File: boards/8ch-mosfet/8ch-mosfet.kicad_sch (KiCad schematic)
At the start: 6 parts, among them U1 ESP32-DEVKITC

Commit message: updated layout with new fuse.
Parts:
- H1, H2, H3, H4, H5: symbol Mechanical:MountingHole -> Mechanical:MountingHole_Pad
- U1: footprint gnarboard:ESP32-DevKitC -> yarrboard:ESP32-DevKitC
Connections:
- no-connect marks 13 -> 18
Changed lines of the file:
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@@
   (no_connect (at 223.52 92.71))
   (no_connect (at 185.42 57.15))
+  (no_connect (at 15.24 195.58))
   (no_connect (at 223.52 97.79))
   (no_connect (at 185.42 95.25))
@@
   (no_connect (at 185.42 59.69))
   (no_connect (at 223.52 64.77))
+  (no_connect (at 15.24 180.34))
   (no_connect (at 223.52 62.23))
+  (no_connect (at 15.24 165.1))
   (no_connect (at 223.52 100.33))
+  (no_connect (at 15.24 172.72))
   (no_connect (at 223.52 87.63))
   (no_connect (at 185.42 67.31))
+  (no_connect (at 15.24 187.96))
   (no_connect (at 223.52 95.25))
   (wire (pts (xy 181.61 62.23) (xy 185.42 62.23))
@@
     )
   )
-  (symbol (lib_id "Mechanical:MountingHole") (at 15.875 184.785 0) (unit 1)
+  (symbol (lib_id "Mechanical:MountingHole_Pad") (at 15.24 177.8 0) (unit 1)
     (in_bom yes) (on_board yes) (dnp no) (fields_autoplaced)
-    (property "Reference" "H3" (at 18.415 183.515 0)
-      (effects (font (size 1.27 1.27)) (justify left))
-    )
-    (property "Value" "MountingHole" (at 18.415 186.055 0)
-      (effects (font (size 1.27 1.27)) (justify left))
-    )
-    (property "Footprint" "MountingHole:MountingHole_3.2mm_M3_DIN965_Pad" (at 15.875 184.785 0)
-      (effects (font (size 1.27 1.27)) hide)
-    )
-    (property "Datasheet" "~" (at 15.875 184.785 0)
-      (effects (font (size 1.27 1.27)) hide)
-    )
+    (property "Reference" "H3" (at 17.78 176.53 0)
+      (effects (font (size 1.27 1.27)) (justify left))
+    )
+    (property "Value" "MountingHole" (at 17.78 179.07 0)
+      (effects (font (size 1.27 1.27)) (justify left))
+    )
+    (property "Footprint" "MountingHole:MountingHole_3.2mm_M3_DIN965_Pad" (at 15.24 177.8 0)
+      (effects (font (size 1.27 1.27)) hide)
+    )
+    (property "Datasheet" "~" (at 15.24 177.8 0)
+      (effects (font (size 1.27 1.27)) hide)
+    )
+    (pin "1")
     (instances
       (project "8ch-mosfet"
@@
     )
   )
-  (symbol (lib_id "Mechanical:MountingHole") (at 15.875 194.945 0) (unit 1)
+  (symbol (lib_id "Mechanical:MountingHole_Pad") (at 15.24 193.04 0) (unit 1)
     (in_bom yes) (on_board yes) (dnp no) (fields_autoplaced)
-    (property "Reference" "H5" (at 18.415 193.675 0)
-      (effects (font (size 1.27 1.27)) (justify left))
-    )
-    (property "Value" "MountingHole" (at 18.415 196.215 0)
-      (effects (font (size 1.27 1.27)) (justify left))
-    )
-    (property "Footprint" "MountingHole:MountingHole_3.2mm_M3_DIN965_Pad" (at 15.875 194.945 0)
-      (effects (font (size 1.27 1.27)) hide)
-    )
-    (property "Datasheet" "~" (at 15.875 194.945 0)
-      (effects (font (size 1.27 1.27)) hide)
-    )
+    (property "Reference" "H5" (at 17.78 191.77 0)
+      (effects (font (size 1.27 1.27)) (justify left))
+    )
+    (property "Value" "MountingHole" (at 17.78 194.31 0)
+      (effects (font (size 1.27 1.27)) (justify left))
+    )
+    (property "Footprint" "MountingHole:MountingHole_3.2mm_M3_DIN965_Pad" (at 15.24 193.04 0)
+      (effects (font (size 1.27 1.27)) hide)
+    )
+    (property "Datasheet" "~" (at 15.24 193.04 0)
+      (effects (font (size 1.27 1.27)) hide)
+    )
+    (pin "1")
     (instances
       (project "8ch-mosfet"
@@
     )
   )
-  (symbol (lib_id "Mechanical:MountingHole") (at 15.875 179.705 0) (unit 1)
+  (symbol (lib_id "Mechanical:MountingHole_Pad") (at 15.24 170.18 0) (unit 1)
     (in_bom yes) (on_board yes) (dnp no) (fields_autoplaced)
-    (property "Reference" "H2" (at 18.415 178.435 0)
-      (effects (font (size 1.27 1.27)) (justify left))
-    )
-    (property "Value" "MountingHole" (at 18.415 180.975 0)
-      (effects (font (size 1.27 1.27)) (justify left))
-    )
-    (property "Footprint" "MountingHole:MountingHole_3.2mm_M3_DIN965_Pad" (at 15.875 179.705 0)
-      (effects (font (size 1.27 1.27)) hide)
-    )
-    (property "Datasheet" "~" (at 15.875 179.705 0)
-      (effects (font (size 1.27 1.27)) hide)
-    )
+    (property "Reference" "H2" (at 17.78 168.91 0)
+      (effects (font (size 1.27 1.27)) (justify left))
+    )
+    (property "Value" "MountingHole" (at 17.78 171.45 0)
+      (effects (font (size 1.27 1.27)) (justify left))
+    )
+    (property "Footprint" "MountingHole:MountingHole_3.2mm_M3_DIN965_Pad" (at 15.24 170.18 0)
+      (effects (font (size 1.27 1.27)) hide)
+    )
+    (property "Datasheet" "~" (at 15.24 170.18 0)
+      (effects (font (size 1.27 1.27)) hide)
+    )
+    (pin "1")
     (instances
       (project "8ch-mosfet"
@@
       (effects (font (size 1.27 1.27)) hide)
     )
-    (property "Footprint" "gnarboard:ESP32-DevKitC" (at 204.47 49.53 0)
+    (property "Footprint" "yarrboard:ESP32-DevKitC" (at 204.47 49.53 0)
       (effects (font (size 1.27 1.27)))
     )
@@
     )
   )
-  (symbol (lib_id "Mechanical:MountingHole") (at 15.875 174.625 0) (unit 1)
+  (symbol (lib_id "Mechanical:MountingHole_Pad") (at 15.24 162.56 0) (unit 1)
     (in_bom yes) (on_board yes) (dnp no) (fields_autoplaced)
-    (property "Reference" "H1" (at 18.415 173.355 0)
-      (effects (font (size 1.27 1.27)) (justify left))
-    )
-    (property "Value" "MountingHole" (at 18.415 175.895 0)
-      (effects (font (size 1.27 1.27)) (justify left))
-    )
-    (property "Footprint" "MountingHole:MountingHole_3.2mm_M3_DIN965_Pad" (at 15.875 174.625 0)
-      (effects (font (size 1.27 1.27)) hide)
-    )
-    (property "Datasheet" "~" (at 15.875 174.625 0)
-      (effects (font (size 1.27 1.27)) hide)
-    )
+    (property "Reference" "H1" (at 17.78 161.29 0)
+      (effects (font (size 1.27 1.27)) (justify left))
+    )
+    (property "Value" "MountingHole" (at 17.78 163.83 0)
+      (effects (font (size 1.27 1.27)) (justify left))
+    )
+    (property "Footprint" "MountingHole:MountingHole_3.2mm_M3_DIN965_Pad" (at 15.24 162.56 0)
+      (effects (font (size 1.27 1.27)) hide)
+    )
+    (property "Datasheet" "~" (at 15.24 162.56 0)
+      (effects (font (size 1.27 1.27)) hide)
+    )
+    (pin "1")
     (instances
       (project "8ch-mosfet"
@@
     )
   )
-  (symbol (lib_id "Mechanical:MountingHole") (at 15.875 189.865 0) (unit 1)
+  (symbol (lib_id "Mechanical:MountingHole_Pad") (at 15.24 185.42 0) (unit 1)
     (in_bom yes) (on_board yes) (dnp no) (fields_autoplaced)
-    (property "Reference" "H4" (at 18.415 188.595 0)
-      (effects (font (size 1.27 1.27)) (justify left))
-    )
-    (property "Value" "MountingHole" (at 18.415 191.135 0)
-      (effects (font (size 1.27 1.27)) (justify left))
-    )
-    (property "Footprint" "MountingHole:MountingHole_3.2mm_M3_DIN965_Pad" (at 15.875 189.865 0)
-      (effects (font (size 1.27 1.27)) hide)
-    )
-    (property "Datasheet" "~" (at 15.875 189.865 0)
-      (effects (font (size 1.27 1.27)) hide)
-    )
-    (instances
-      (project "8ch-mosfet"
+    (property "Reference" "H4" (at 17.78 184.15 0)
+      (effects (font (size 1.27 1.27)) (justify left))
+    )
+    (property "Value" "MountingHole" (at 17.78 186.69 0)
+      (effects (font (size 1.27 1.27)) (justify left))
+    )
+    (property "Footprint" "MountingHole:MountingHole_3.2mm_M3_DIN965_Pad" (at 15.24 185.42 0)
+      (effects (font (size 1.27 1.27)) hide)
+    )
+    (property "Datasheet" "~" (at 15.24 185.42 0)
+      (effects (font (size 1.27 1.27)) hide)
+    )
+    (pin "1")
+    (instances
+      (project "8ch-mosfet"

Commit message: prepared 8ch mosfet for production
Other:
- company: (none) -> https://github.com/hoeken/yarrboard
- title: (none) -> Yarrboard 8ch Mosfet Driver
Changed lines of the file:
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@@
   (paper "A4")
   (title_block
+    (title "Yarrboard 8ch Mosfet Driver")
     (rev "B")
+    (company "https://github.com/hoeken/yarrboard")
   )
   (junction (at 241.3 69.85) (diameter 0) (color 0 0 0 0)

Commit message: updated BOM
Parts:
- H1, H2, H3, H4, H5: now not fitted; now left out of the parts list
- U1: Mouser (none) -> 356-ESP32-DEVKITC32E; Vendor 356-ESP32-DEVKITC32E -> (none)
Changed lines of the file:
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@@
   )
   (symbol (lib_id "Mechanical:MountingHole_Pad") (at 15.24 177.8 0) (unit 1)
-    (in_bom yes) (on_board yes) (dnp no) (fields_autoplaced)
+    (in_bom no) (on_board yes) (dnp yes) (fields_autoplaced)
     (property "Reference" "H3" (at 17.78 176.53 0)
       (effects (font (size 1.27 1.27)) (justify left))
@@
   )
   (symbol (lib_id "Mechanical:MountingHole_Pad") (at 15.24 193.04 0) (unit 1)
-    (in_bom yes) (on_board yes) (dnp no) (fields_autoplaced)
+    (in_bom no) (on_board yes) (dnp yes) (fields_autoplaced)
     (property "Reference" "H5" (at 17.78 191.77 0)
       (effects (font (size 1.27 1.27)) (justify left))
@@
   )
   (symbol (lib_id "Mechanical:MountingHole_Pad") (at 15.24 170.18 0) (unit 1)
-    (in_bom yes) (on_board yes) (dnp no) (fields_autoplaced)
+    (in_bom no) (on_board yes) (dnp yes) (fields_autoplaced)
     (property "Reference" "H2" (at 17.78 168.91 0)
       (effects (font (size 1.27 1.27)) (justify left))
@@
       (effects (font (size 1.27 1.27)) hide)
     )
-    (property "Vendor" "356-ESP32-DEVKITC32E " (at 204.47 76.2 0)
+    (property "Mouser" "356-ESP32-DEVKITC32E " (at 204.47 76.2 0)
       (effects (font (size 1.27 1.27)) hide)
     )
@@
   )
   (symbol (lib_id "Mechanical:MountingHole_Pad") (at 15.24 162.56 0) (unit 1)
-    (in_bom yes) (on_board yes) (dnp no) (fields_autoplaced)
+    (in_bom no) (on_board yes) (dnp yes) (fields_autoplaced)
     (property "Reference" "H1" (at 17.78 161.29 0)
       (effects (font (size 1.27 1.27)) (justify left))
@@
   )
   (symbol (lib_id "Mechanical:MountingHole_Pad") (at 15.24 185.42 0) (unit 1)
-    (in_bom yes) (on_board yes) (dnp no) (fields_autoplaced)
+    (in_bom no) (on_board yes) (dnp yes) (fields_autoplaced)
     (property "Reference" "H4" (at 17.78 184.15 0)
       (effects (font (size 1.27 1.27)) (justify left))

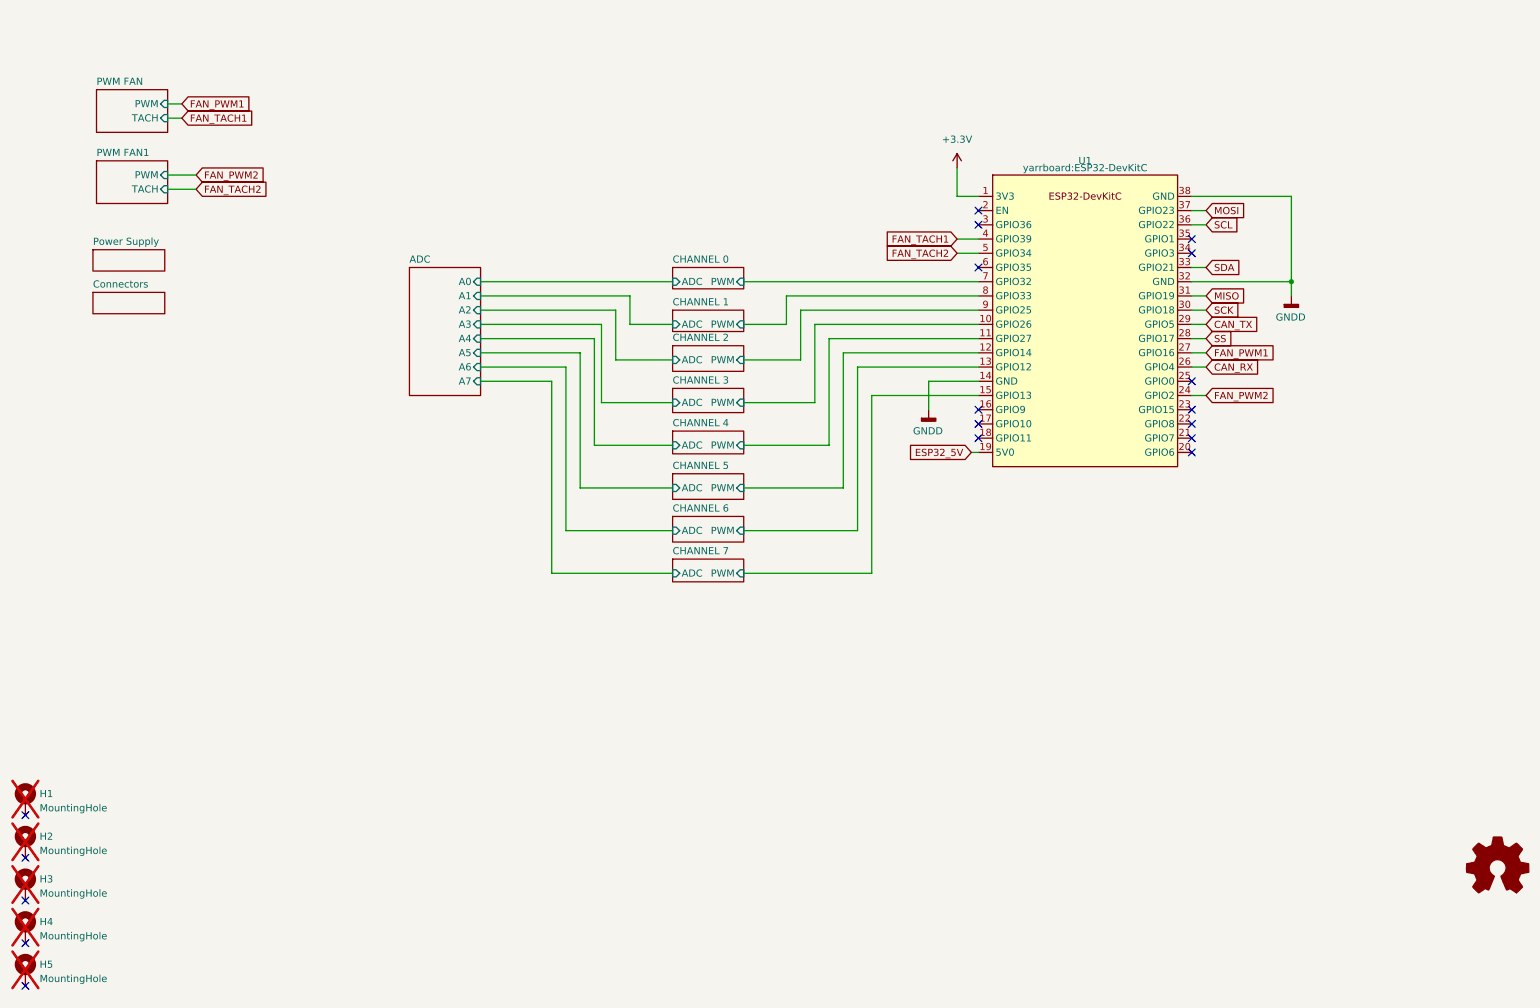
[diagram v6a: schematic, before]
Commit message: oof, working from the wrong copy, had to redo some stuff
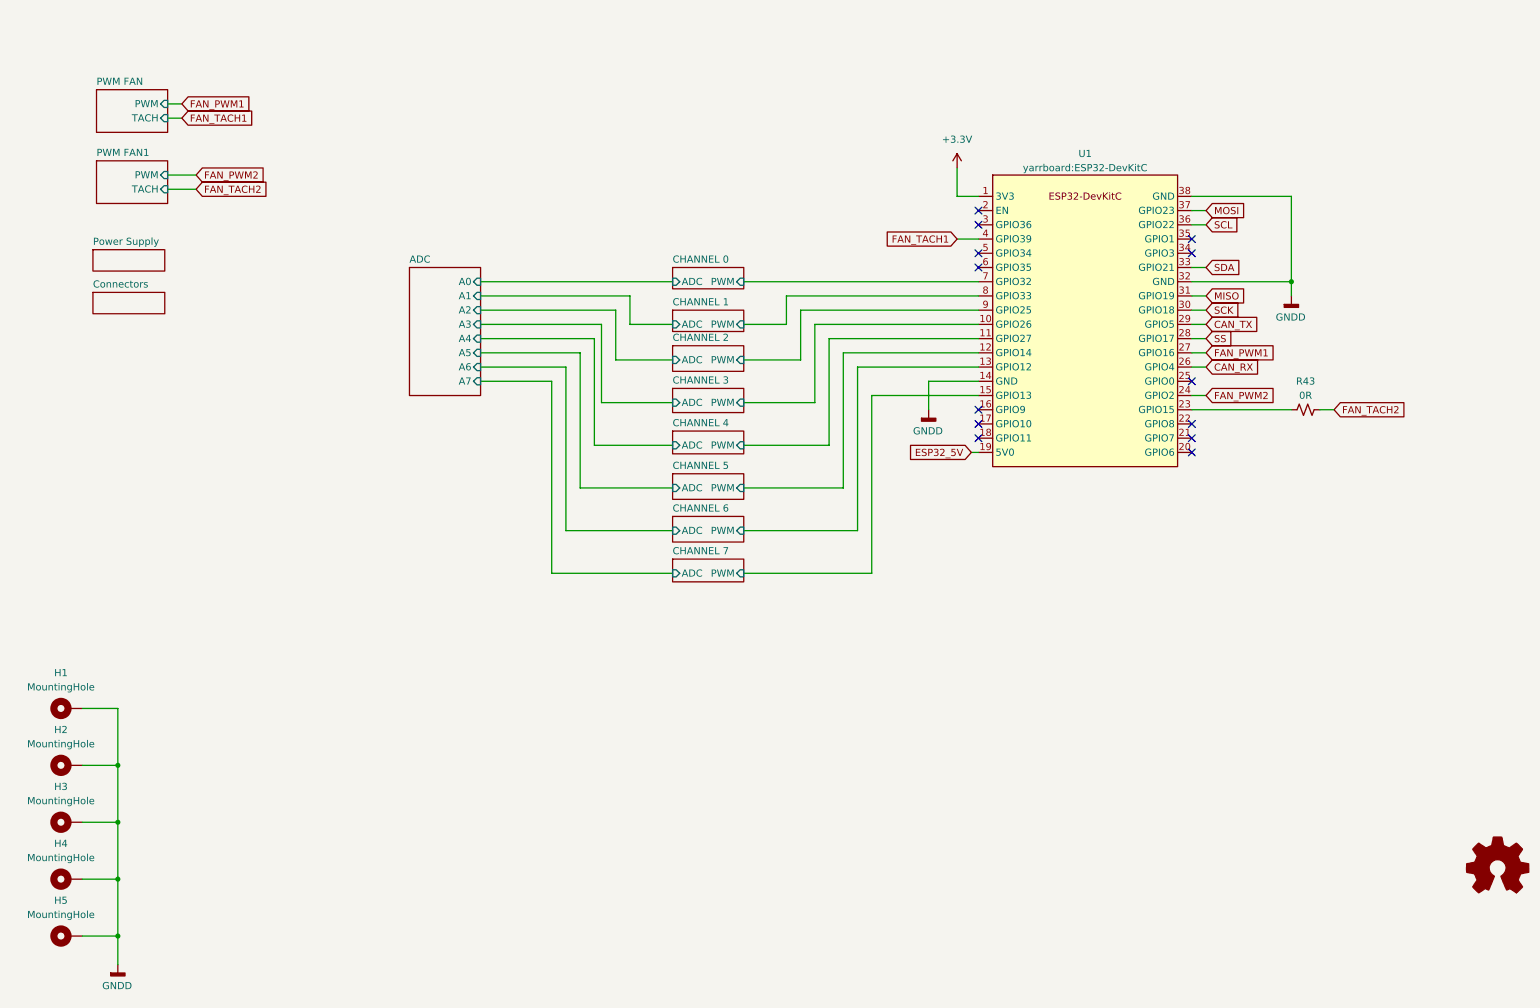
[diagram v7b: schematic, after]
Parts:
- added R43: 0R, Resistor_SMD:R_0805_2012Metric_Pad1.20x1.40mm_HandSolder, symbol Device:R_Small_US
- H1, H2, H3, H4, H5: now fitted
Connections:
- net FAN_TACH2: now also R43.2; no longer U1.5 (GPIO34)
- net GNDD: now also H1.1, H2.1, H3.1, H4.1, H5.1
- net at U1.23 (GPIO15): now also R43.1
- no-connect marks 18 -> 13
